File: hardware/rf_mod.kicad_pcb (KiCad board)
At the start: 4 copper layers, 100 x 100 mm, 170 parts, among them J1001 SMA, J1002 SMA, J1003 Pmod, J101 SMA, J102 SMA, J103 SMA, J1201 SMA, J1202 SMA, J1301 SMA, J1302 SMA, J1303 SMA, J201 SMA, J202 SMA, J401 SMA, J402 SMA, J501 SMA, J502 SMA, J701 SMA, J702 SMA, J703 SMA, J801 SMA, J802 SMA, J803 SMA, J901 USB-C, J902 SMA, Q1001 AO3401A, Q1201 AO3401A, Q1301 AO3401A, Q501 AO3401A, Q701 AO3401A, Q801 AO3401A, SW1001 ON, SW1201 ON, SW1301 ON, SW501 ON, SW701 ON, SW801 ON, U1001 3.3V, U1002 MAX2871, U1201 GALI-84+, U1301 TRF3722, U1302 3.3V, U501 QPL9547, U701 3.3V, U702 ADL5350, U801 3.3V, U802 ADL5350, U901 MT3608, U902 3.3V, U903 74LVC1G17, X901 25 MHz

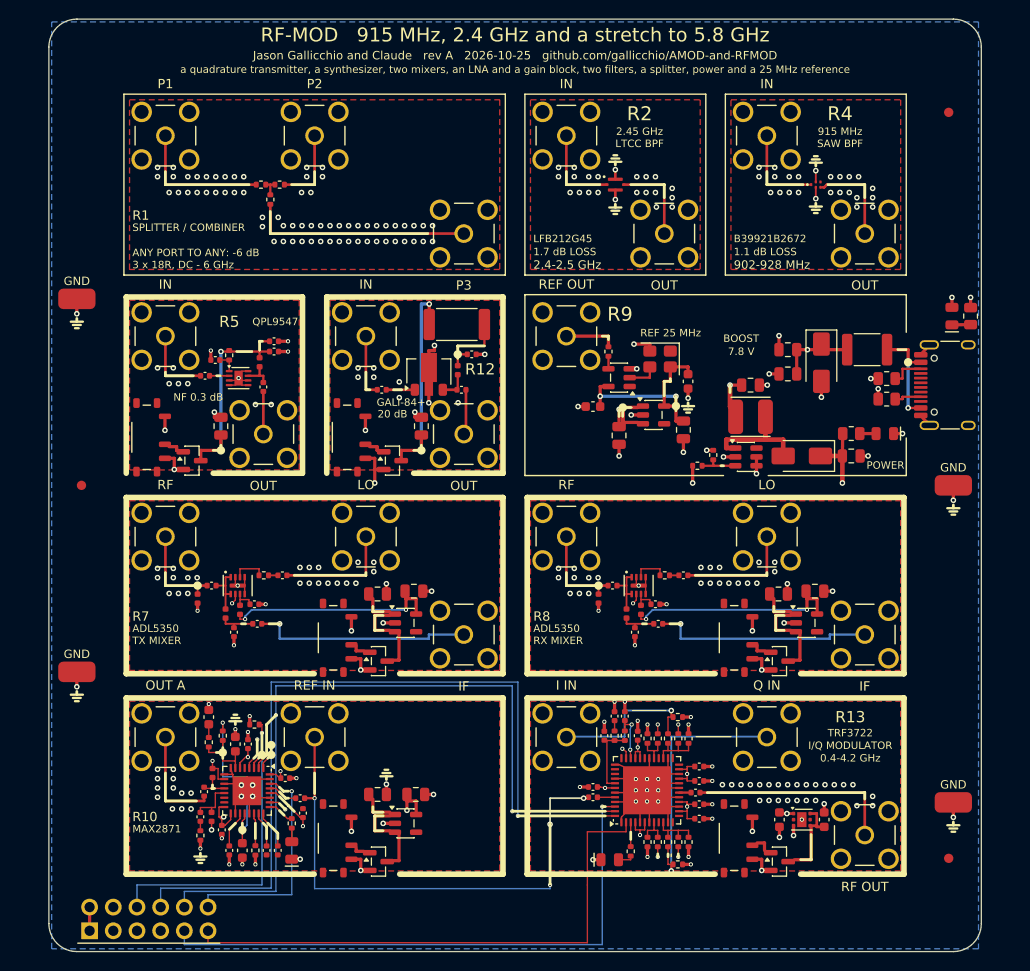
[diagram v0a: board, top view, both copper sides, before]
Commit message: Silkscreen says what each tile is and whose jack is whose: jack names on their own tile's frame, titles in words on the top frame, ranges and levels placed inside; tutorial section numbers off the boards; README tables of every tile (what, chip link, specs, limits, experiments, use, what to buy) and handbook entries as tables with a picture of each tile, both from boards/tile_docs.py
Co-Authored-By: Claude Opus 5.5 <noreply@anthropic.com>
Claude-Session: https://claude.ai/code/session_01RKeoKvFFzjk3cEBLCXXHnB
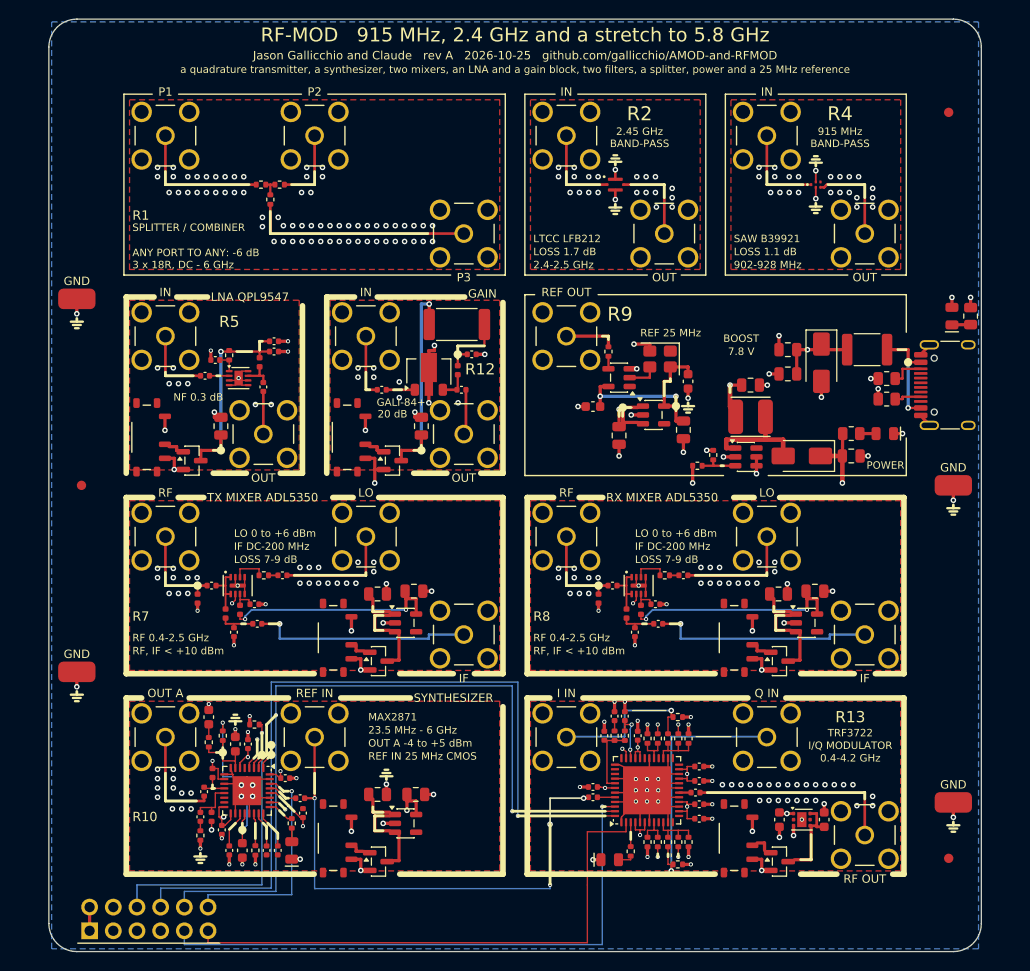
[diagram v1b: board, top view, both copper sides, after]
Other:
- board text added: "23.5 MHz - 6 GHz"
- board text added: "BAND-PASS"
- board text added: "GAIN"
- board text added: "IF DC-200 MHz"
- board text added: "LNA QPL9547"
- board text added: "LO 0 to +6 dBm"
- board text added: "LOSS 1.1 dB"
- board text added: "LOSS 1.7 dB"
- board text added: "LOSS 7-9 dB"
- board text added: "LTCC LFB212"
- board text added: "OUT A -4 to +5 dBm"
- board text added: "REF IN 25 MHz CMOS"
- board text added: "RF 0.4-2.5 GHz"
- board text added: "RF, IF < +10 dBm"
- board text added: "RX MIXER ADL5350"
- board text added: "SAW B39921"
- board text added: "SYNTHESIZER"
- board text added: "TX MIXER ADL5350"
- board text removed: "1.1 dB LOSS"
- board text removed: "1.7 dB LOSS"
- board text removed: "ADL5350"
- board text removed: "B39921B2672"
- board text removed: "LFB212G45"
- board text removed: "LTCC BPF"
- board text removed: "QPL9547"
- board text removed: "RX MIXER"
- board text removed: "SAW BPF"
- board text removed: "TX MIXER"

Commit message: RF-MOD: R1 is a diode-ring mixer (ADEX-10L+, 10-1000 MHz, LO +4 dBm; its baluns and ring of four diodes drawn on the silk) in the splitter's place; R10's RFOUTA- comes out on OUT A- (bottom-right of its right cell) along a 50 ohm line in the margin under the tile, the top pour following it; OUT A becomes OUT A+
Generators: silk drawings (Tile.draw_line / draw_arc), a top-pour tongue below an RF tile (Tile.pour_below), jack names slide up to 4.5 mm and say what blocks them; footprints, symbols and models for the ADEX-10L+ and the HHM22137A1 coupler.

Co-Authored-By: Claude Opus 5.5 <noreply@anthropic.com>
Claude-Session: https://claude.ai/code/session_01RKeoKvFFzjk3cEBLCXXHnB
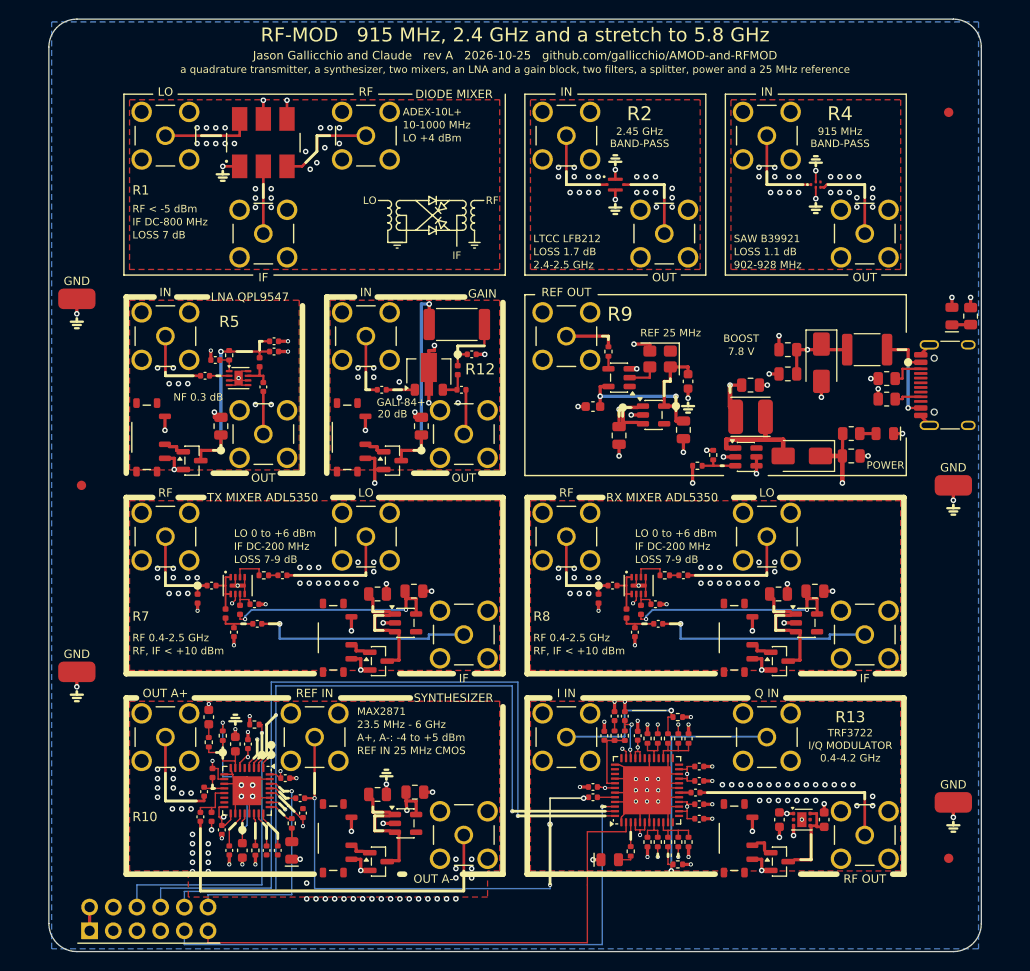
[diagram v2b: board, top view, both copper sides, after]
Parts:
- removed R1006: 5.1k, Resistor_SMD:R_0402_1005Metric
- removed R101, R102, R103: 18R, Resistor_SMD:R_0402_1005Metric
- added J1004: Pmod, amod:PinHeader_2x06_P2.54mm_Horizontal_PZ254R-12-12P, F.Cu at (10.7, 96.5)
- added U101: ADEX-10L+, amod:MiniCircuits_CD542_ADEX-10L, F.Cu at (23.0, 13.2)
- J1003: value Pmod -> SMA; footprint amod:PinHeader_2x06_P2.54mm_Horizontal_PZ254R-12-12P -> amod:SMA_BWSMA-KE-Z001_Vertical
- R1005: value 51R -> 5.1k
- moved J1003 35.0 mm to (44.5, 87.5)
- moved J103 21.5 mm to (23.0, 23.0)
- moved R1005 6.11 mm to (22.1, 89.2)
- moved J102 5.50 mm to (34.0, 12.5)
- moved C1002 0.27 mm to (39.2, 82.9)
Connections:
- C1010 pad 2: /R10_TRM -> /R10_OUTAN
- J1003 pad 1: /PMOD_VCC -> /R10_OUTAN
- J1003 pad 2: /PMOD_VCC -> GND
- J101 pad 1: /R1_P1 -> /R1_LO
- J102 pad 1: /R1_P2 -> /R1_RF
- J103 pad 1: /R1_P3 -> /R1_IF
- R1005 pad 1: /R10_TRM -> /R10_RS
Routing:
- net /R10_OUTAN: track 0.00 -> 41.7 mm
- net /R1_P3: track 23.9 -> 0.00 mm
- net /R1_P1: track 15.0 -> 0.00 mm
- net /R1_RF: track 0.00 -> 10.8 mm
- net /R1_LO: track 0.00 -> 9.75 mm
- net /R1_P2: track 8.49 -> 0.00 mm
- net /R1_IF: track 0.00 -> 7.21 mm
- net GND: track 149.3 -> 154.2 mm, vias 305 -> 299
- net /R1_N: track 2.07 -> 0.00 mm
- net /R10_TRM: track 1.01 -> 0.00 mm
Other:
- board text added: "10-1000 MHz"
- board text added: "A+, A-: -4 to +5 dBm"
- board text added: "ADEX-10L+"
- board text added: "DIODE MIXER"
- board text added: "IF DC-800 MHz"
- board text added: "LO +4 dBm"
- board text added: "LOSS 7 dB"
- board text added: "OUT A+"
- board text added: "OUT A-"
- board text added: "RF < -5 dBm"
- board text removed: "3 x 18R, DC - 6 GHz"
- board text removed: "ANY PORT TO ANY: -6 dB"
- board text removed: "OUT A"
- board text removed: "OUT A -4 to +5 dBm"
- board text removed: "P1"
- board text removed: "P2"
- board text removed: "P3"
- board text removed: "SPLITTER / COMBINER"

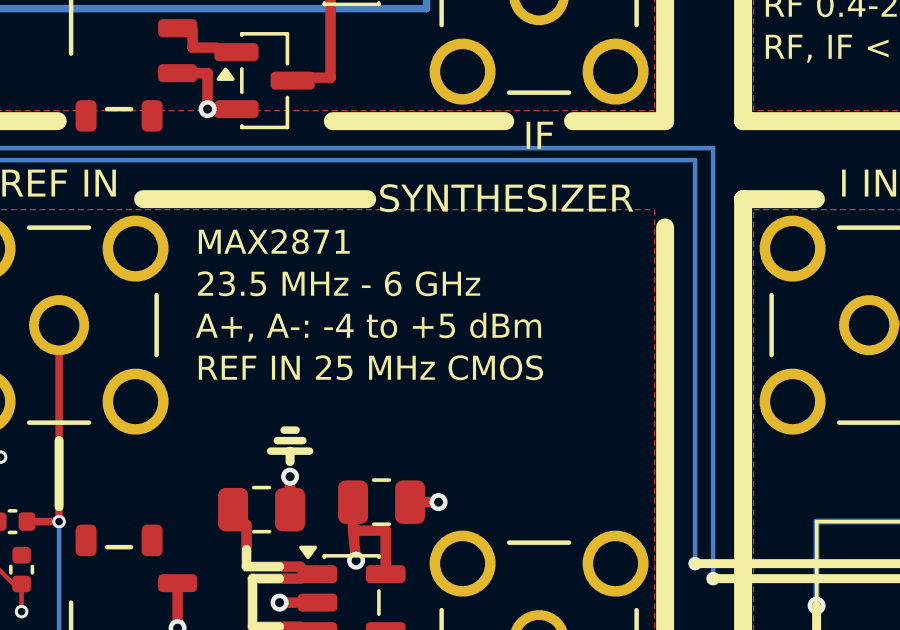
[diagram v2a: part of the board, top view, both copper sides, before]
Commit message: RF-MOD-2: X5 is a dual directional coupler (two HHM22137A1 back to back, 0.6-3.5 GHz, FWD and REFL 25 dB down, 20 dB directivity) in the splitter's place; X3's RFOUTA- on OUT A- (its right cell's bottom-right) so OUT A+ and OUT A- are X1's and X2's LOs, REF IN moved to the right cell's top-left with its line on the back; IO5 and IO6 lowered in the margin under OUT A-'s line
Co-Authored-By: Claude Opus 5.5 <noreply@anthropic.com>
Claude-Session: https://claude.ai/code/session_01RKeoKvFFzjk3cEBLCXXHnB
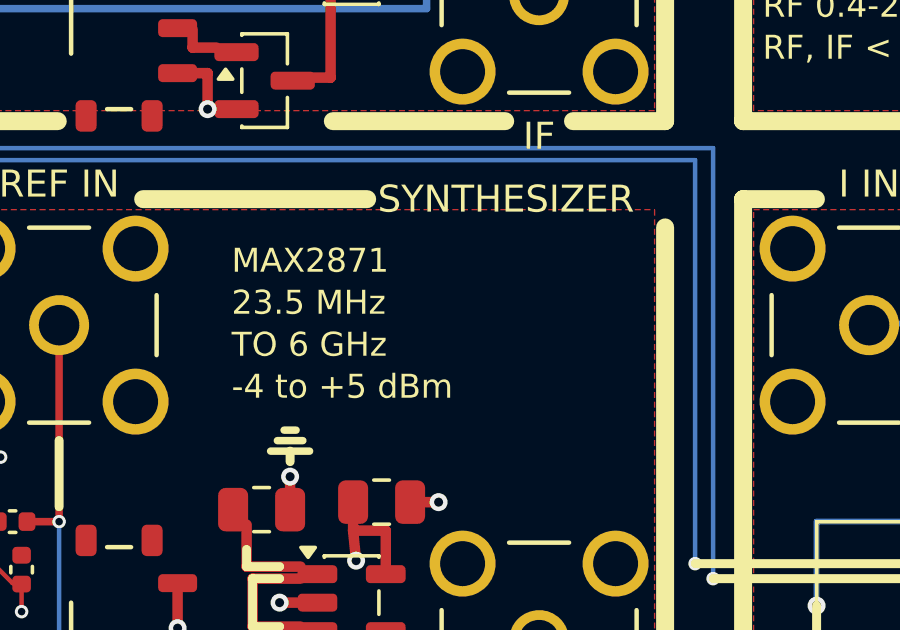
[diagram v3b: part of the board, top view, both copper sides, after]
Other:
- board text added: "-4 to +5 dBm"
- board text added: "23.5 MHz"
- board text added: "TO 6 GHz"
- board text removed: "23.5 MHz - 6 GHz"
- board text removed: "A+, A-: -4 to +5 dBm"
- board text removed: "REF IN 25 MHz CMOS"
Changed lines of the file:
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@@
 	)
 	(gr_text "MAX2871"
-		(at 33.049999 74.25 0)
+		(at 34.25 74.85 0)
 		(layer "F.SilkS")
 		(effects
@@
 		)
 	)
-	(gr_text "23.5 MHz - 6 GHz"
-		(at 33.049999 75.65 0)
+	(gr_text "23.5 MHz"
+		(at 34.25 76.25 0)
 		(layer "F.SilkS")
 		(effects
@@
 		)
 	)
-	(gr_text "A+, A-: -4 to +5 dBm"
-		(at 33.049999 77.05 0)
+	(gr_text "TO 6 GHz"
+		(at 34.25 77.649999 0)
 		(layer "F.SilkS")
 		(effects
@@
 		)
 	)
-	(gr_text "REF IN 25 MHz CMOS"
-		(at 33.049999 78.45 0)
+	(gr_text "-4 to +5 dBm"
+		(at 34.25 79.05 0)
 		(layer "F.SilkS")
 		(effects

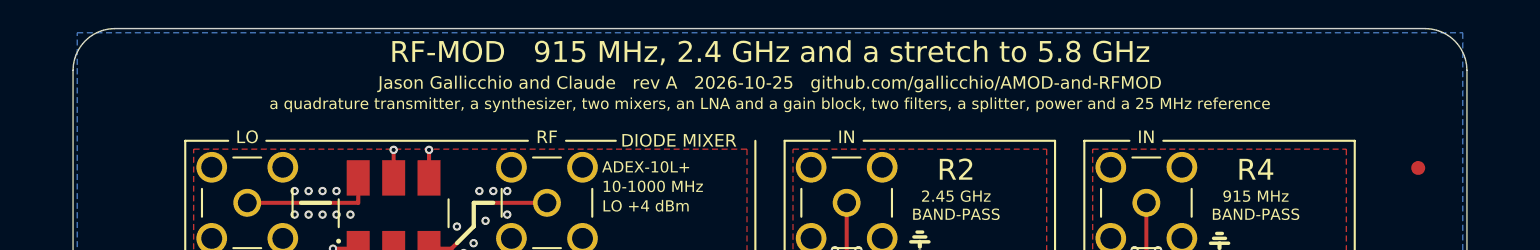
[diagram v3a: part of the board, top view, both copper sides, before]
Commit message: RF-MOD and RF-MOD-2 subtitles (on the copper and the schematic) without the splitters; rebuilt
Co-Authored-By: Claude Opus 5.5 <noreply@anthropic.com>
Claude-Session: https://claude.ai/code/session_01RKeoKvFFzjk3cEBLCXXHnB
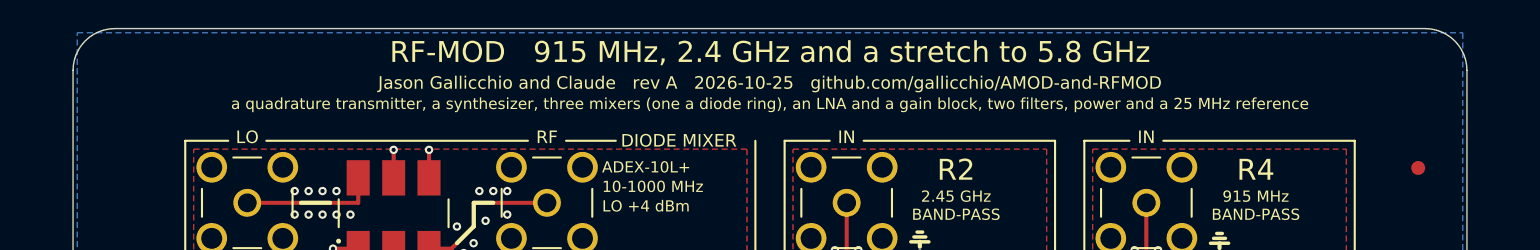
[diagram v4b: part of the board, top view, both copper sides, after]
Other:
- board text added: "a quadrature transmitter, a synthesizer, three mixers (one a diode ring), an LNA and a gain block, two filters, power and a 25 MHz reference"
- board text removed: "a quadrature transmitter, a synthesizer, two mixers, an LNA and a gain block, two filters, a splitter, power and a 25 MHz reference"
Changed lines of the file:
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@@
 		)
 	)
-	(gr_text "a quadrature transmitter, a synthesizer, two mixers, an LNA and a gain block, two filters, a splitter, power and a 25 MHz reference"
+	(gr_text "a quadrature transmitter, a synthesizer, three mixers (one a diode ring), an LNA and a gain block, two filters, power and a 25 MHz reference"
 		(at 50 5.4 0)
 		(layer "F.SilkS")
